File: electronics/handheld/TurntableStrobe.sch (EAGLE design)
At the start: 17 parts, among them J1 ISP, Q1 12MHz, Q2 BJT-NPNSOT23, U1 TINY25, U2 LM2665

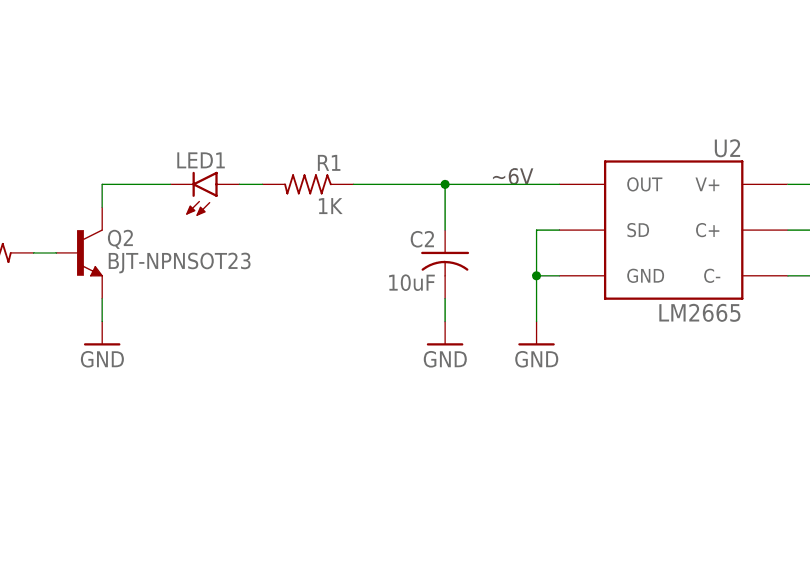
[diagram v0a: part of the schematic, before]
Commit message: updated supply caps
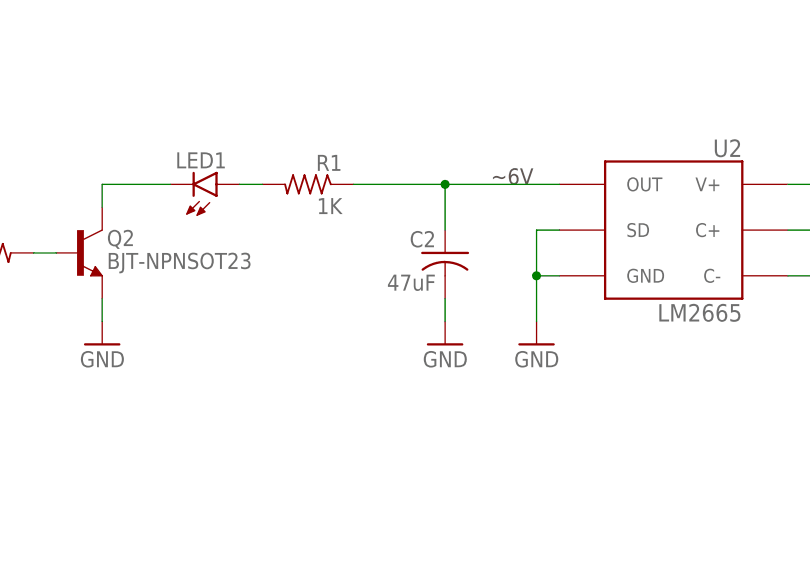
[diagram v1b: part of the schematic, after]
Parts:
- C2: value 10uF -> 47uF
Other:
- note added: "Q: Unsafe to expose GPIO to 6V w/ leakage current?"
- note removed: "Q: Does a large supply cap help?"
- note removed: "Q: Is it unsafe to drive pin directly?"
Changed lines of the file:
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@@
 <part name="GND5" library="mes" deviceset="GND" device=""/>
 <part name="R4" library="rcl" deviceset="R-US_" device="R0603" value="10K"/>
-<part name="C2" library="rcl" deviceset="C-US" device="C0603" value="10uF"/>
+<part name="C2" library="rcl" deviceset="C-US" device="C0603" value="47uF"/>
 <part name="Q2" library="bt_transistor" deviceset="BJT-NPN" device="SOT23" value="BJT-NPNSOT23"/>
 <part name="GND6" library="mes" deviceset="GND" device=""/>
@@
 <text x="231.14" y="17.78" size="3.81" layer="94">R0.4</text>
 <text x="208.28" y="63.5" size="1.778" layer="90">Q: Can 47uF capacitors be used?</text>
-<text x="195.58" y="88.9" size="1.778" layer="90">Q: Does a large supply cap help?</text>
-<text x="73.66" y="71.12" size="1.778" layer="90">Q: Is it unsafe to drive pin directly?</text>
+<text x="86.36" y="48.26" size="1.778" layer="90">Q: Unsafe to expose GPIO to 6V w/ leakage current?</text>
 </plain>
 <instances>
